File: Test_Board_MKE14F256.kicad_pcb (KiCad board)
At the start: 4 copper layers, 62.8 x 49.7 mm, 115 parts, among them P1 CONN_01X02, P2 CONN_01X04, P28 CONN_01X04, P3 CONN_01X02, P4 CONN_01X04, P5 CONN_01X05, P6 CONN_01X04, U1 TS30042, U2 NCP700B, U3 MIC2288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

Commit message: Complete... Still some things to check
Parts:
- C21, C22, C25, C26: value 18p -> 470p
- R29, R30, R31, R32: value ??? -> 5
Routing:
- net GND: track 161.3 -> 196.6 mm, vias 45 -> 69
- net Net-(C12-Pad1): track 35.5 -> 36.0 mm

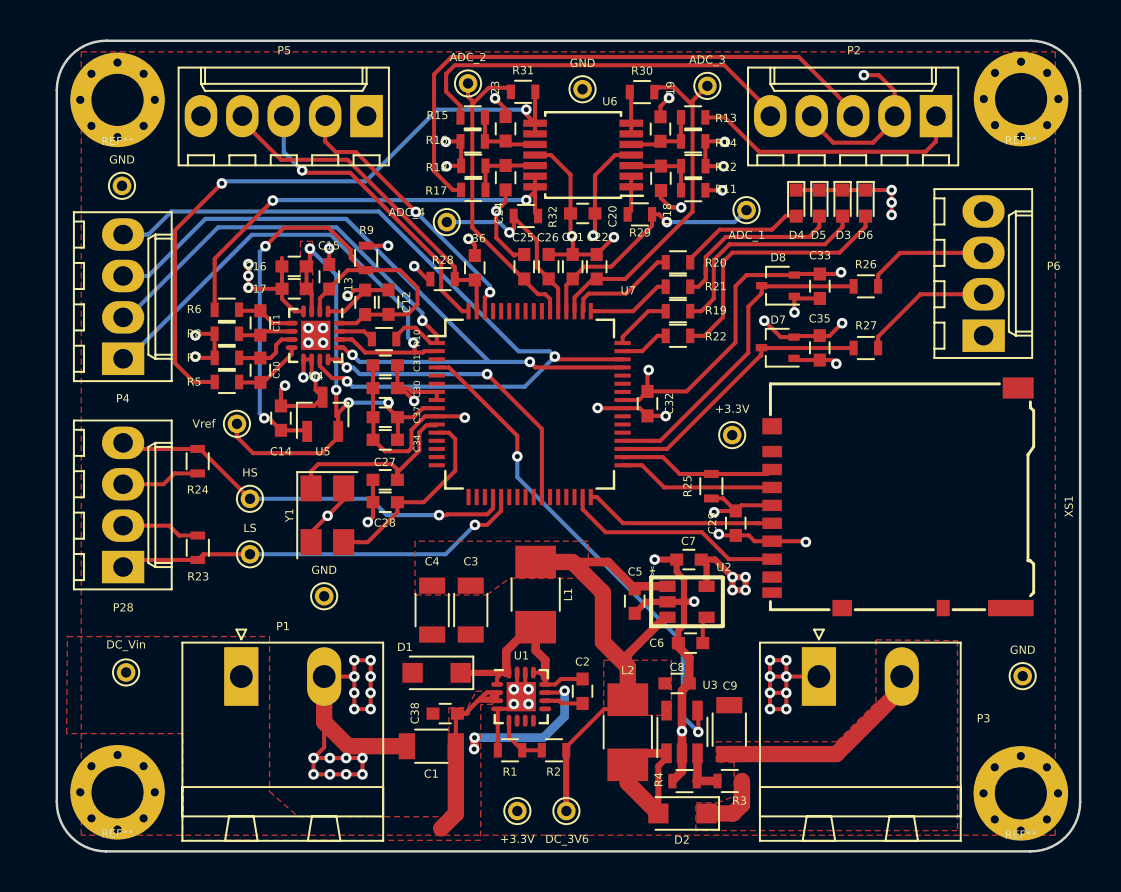
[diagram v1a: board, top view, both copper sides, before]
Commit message: corrected some mistakes listed in the email
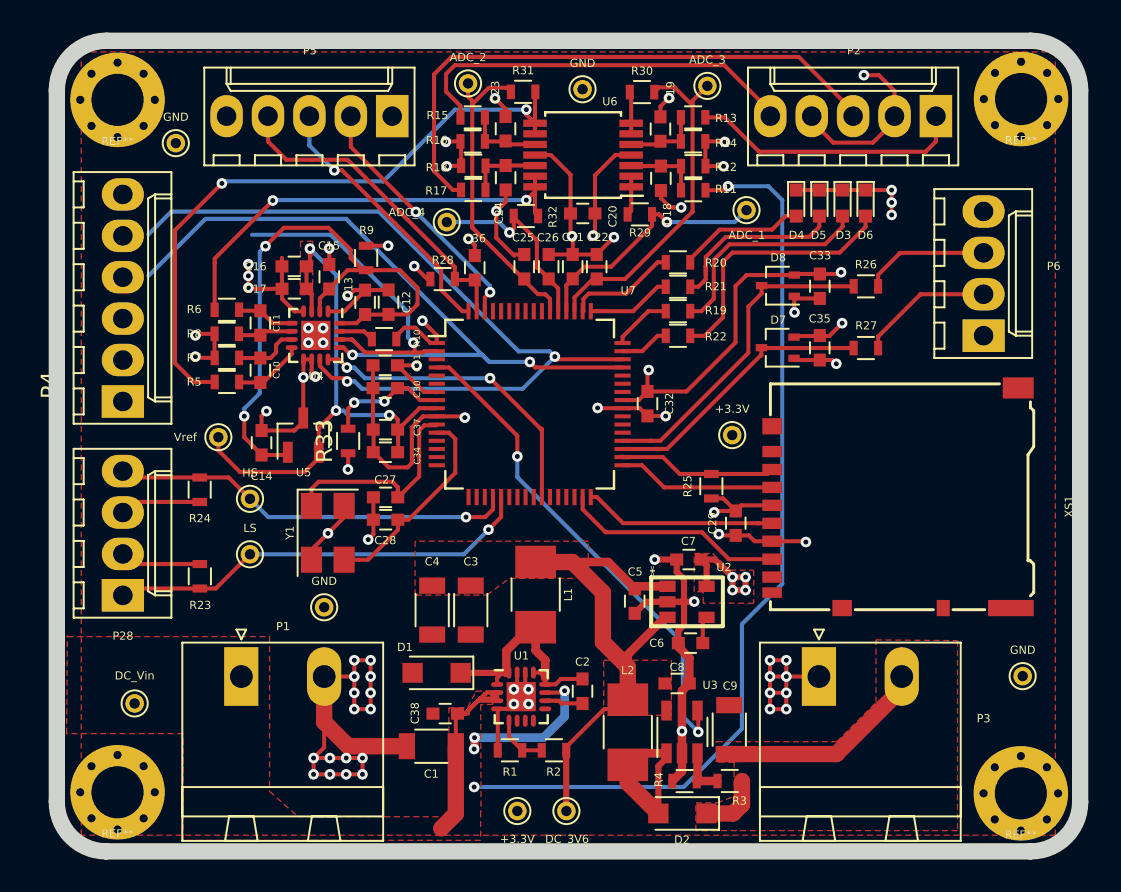
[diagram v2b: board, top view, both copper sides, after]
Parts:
- added R33: 5, Resistors_SMD:R_0603, F.Cu at (154.6, 77.0)
- P4: value CONN_01X04 -> CONN_01X06; footprint Connectors_Molex:Molex_KK-6410-04_04x2.54mm_Straight -> Connectors_Molex:Molex_KK-6410-06_06x2.54mm_Straight
- moved GND 4.21 mm to (144.1, 58.8)
- moved P4 2.62 mm to (140.8, 74.6)
- moved DC_Vin 1.97 mm to (141.5, 93.2)
- moved C14 1.92 mm to (149.3, 77.2)
- moved R23 1.75 mm to (145.5, 85.3)
- moved R24 1.75 mm to (145.5, 80.0)
- moved U5 1.75 mm to (151.9, 76.7)
- moved P28 1.73 mm to (140.8, 86.5)
- moved P5 1.57 mm to (157.3, 57.1)
- moved Vref 1.40 mm to (146.7, 76.8)
- moved C28 1.08 mm to (156.9, 81.9)
- moved Y1 1.08 mm to (153.4, 82.7)
- moved C27 1.08 mm to (156.9, 80.5)
- moved C34 0.76 mm to (156.9, 77.7)
- moved C37 0.76 mm to (156.9, 76.4)
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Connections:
- C30 pad 2: +3V3 -> Net-(C30-Pad2)
- R11 pad 1: +3V3 -> DC_Vin
- U7 pad 8: +3V3 -> Net-(C30-Pad2)
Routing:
- net DC_Vin: track 25.2 -> 81.7 mm, vias 3 -> 5
- net ADC_SPI1_SDO: track 28.3 -> 5.01 mm
- net ADC_SPI1_SCLK: track 31.6 -> 20.5 mm
- net Net-(C30-Pad2): track 0.00 -> 7.52 mm, vias 0 -> 2
- net +3V3: track 55.2 -> 51.4 mm, vias 14 -> 13
- net GND: track 196.6 -> 199.5 mm
- net SWD_DIO_TGTMCU: track 18.5 -> 16.5 mm
- net Vref: track 33.2 -> 35.2 mm, vias 4 -> 3
- net Net-(C12-Pad1): track 36.0 -> 37.7 mm
- net Net-(C27-Pad1): track 12.2 -> 13.8 mm
- net ADC_SPI1_CS0: track 45.7 -> 44.1 mm
- net ADC_SPI1_MOSI_ADC_CH_SEL: track 51.1 -> 49.6 mm
- net SWD_CLK: track 17.0 -> 15.6 mm
- net PWM_LS: track 25.5 -> 26.4 mm
- net SWD_RESET: track 21.0 -> 20.2 mm
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- added copper zone on F.Cu, net +3V3
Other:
- outline, holes or cut-outs redrawn

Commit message: V1.0
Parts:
- added D10: D_Schottky, .pretty:D_SOD-123, F.Cu at (169.3, 100.0)
- added D9: D_Zener_Small, Diodes_SMD:D_SOD-323, F.Cu at (165.1, 100.0)
- added R34: 30k, Resistors_SMD:R_0603, F.Cu at (164.5, 97.7)
- added R35: 10k, Resistors_SMD:R_0603, F.Cu at (167.3, 97.7)
- U1: value TS30042 -> TS3004
- U3: footprint TO_SOT_Packages_SMD:TSOT-23-5 -> Footprints:TSOP-5
- moved +3.3V 18.1 mm to (151.9, 87.2)
- moved DC_3V6 10.8 mm to (169.2, 89.0)
- moved GND 2.70 mm to (155.8, 87.2)
- moved GND 1.04 mm to (195.3, 92.2)
- moved P1 0.32 mm to (148.1, 91.2)
- moved P3 0.32 mm to (183.5, 91.2)
- moved C8 0.23 mm to (175.0, 91.8)
- moved REF** 0.14 mm to (195.8, 56.2)
- moved R4 0.13 mm to (175.3, 98.0)
- moved REF** 0.13 mm to (195.8, 98.5)
- moved REF** 0.08 mm to (140.5, 56.2)
- moved D2 0.07 mm to (175.1, 100.0)
- moved GND 0.06 mm to (144.1, 58.7)
- moved REF** 0.06 mm to (140.5, 98.5)
- turned U3 to 0 degrees
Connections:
- P4 pad 1: ADC_SPI1_SCLK -> +3V3
- P4 pad 2: ADC_SPI1_SDO -> ADC_SPI1_SCLK
- P4 pad 3: ADC_SPI1_CS0 -> ADC_SPI1_SDO
- P4 pad 4: ADC_SPI1_MOSI_ADC_CH_SEL -> ADC_SPI1_CS1
- P4 pad 5: GND -> ADC_SPI1_MOSI_ADC_CH_SEL
- U7 pad 38: Net-(U7-Pad38) -> ADC_SPI1_CS1
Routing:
- net ADC_SPI1_CS1: track 0.00 -> 37.6 mm, vias 0 -> 1
- net ADC_SPI1_CS0: track 44.1 -> 18.3 mm
- net ADC_SPI1_SDO: track 5.01 -> 28.6 mm
- net ADC_SPI1_SCLK: track 20.5 -> 31.7 mm
- net Net-(D10-Pad1): track 0.00 -> 10.1 mm
- net DC_3V6: track 35.4 -> 42.7 mm
- net ADC_SPI1_MOSI_ADC_CH_SEL: track 49.6 -> 53.7 mm
- net DC_Vin: track 81.7 -> 84.3 mm
- net GND: track 199.5 -> 201.6 mm, vias 69 -> 71
- net Net-(C12-Pad1): track 37.7 -> 35.9 mm
- net +3V3: track 51.4 -> 52.2 mm
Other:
- net class Default: clearance 0.2 -> 0.154
- rule pad_to_mask_clearance: 0.2 -> 0.13
- rule trace_clearance: 0.2 -> 0.154
